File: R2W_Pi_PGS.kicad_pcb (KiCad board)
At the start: 2 copper layers, 33 parts, among them J1 USB_OTG, J2 USB_OTG, U1 PAM2306AYPKE, U2 AP7115-25SEG, U3 DDR2_SODIMM_CM_3_Lite, U4 1040310811

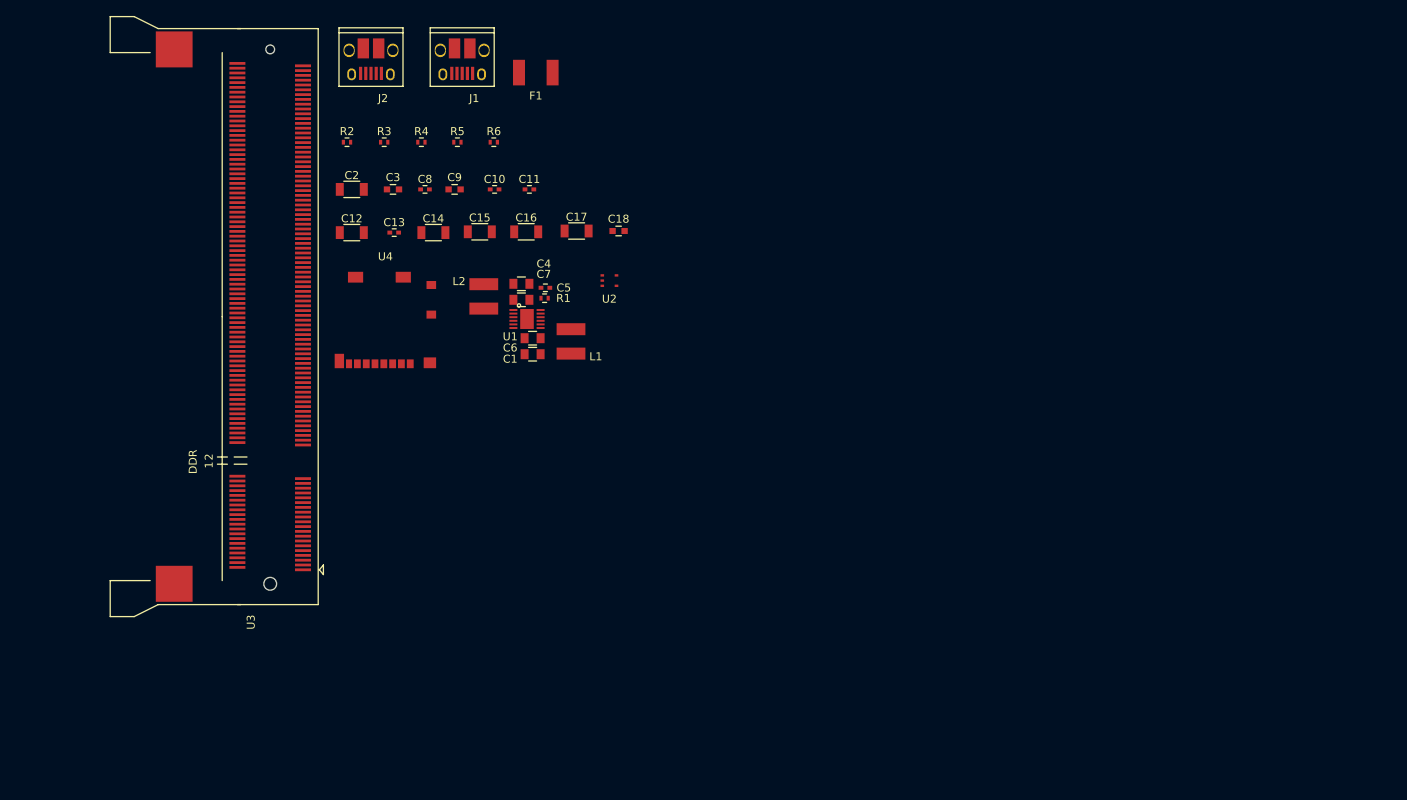
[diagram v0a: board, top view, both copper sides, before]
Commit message: Added screen and buttons
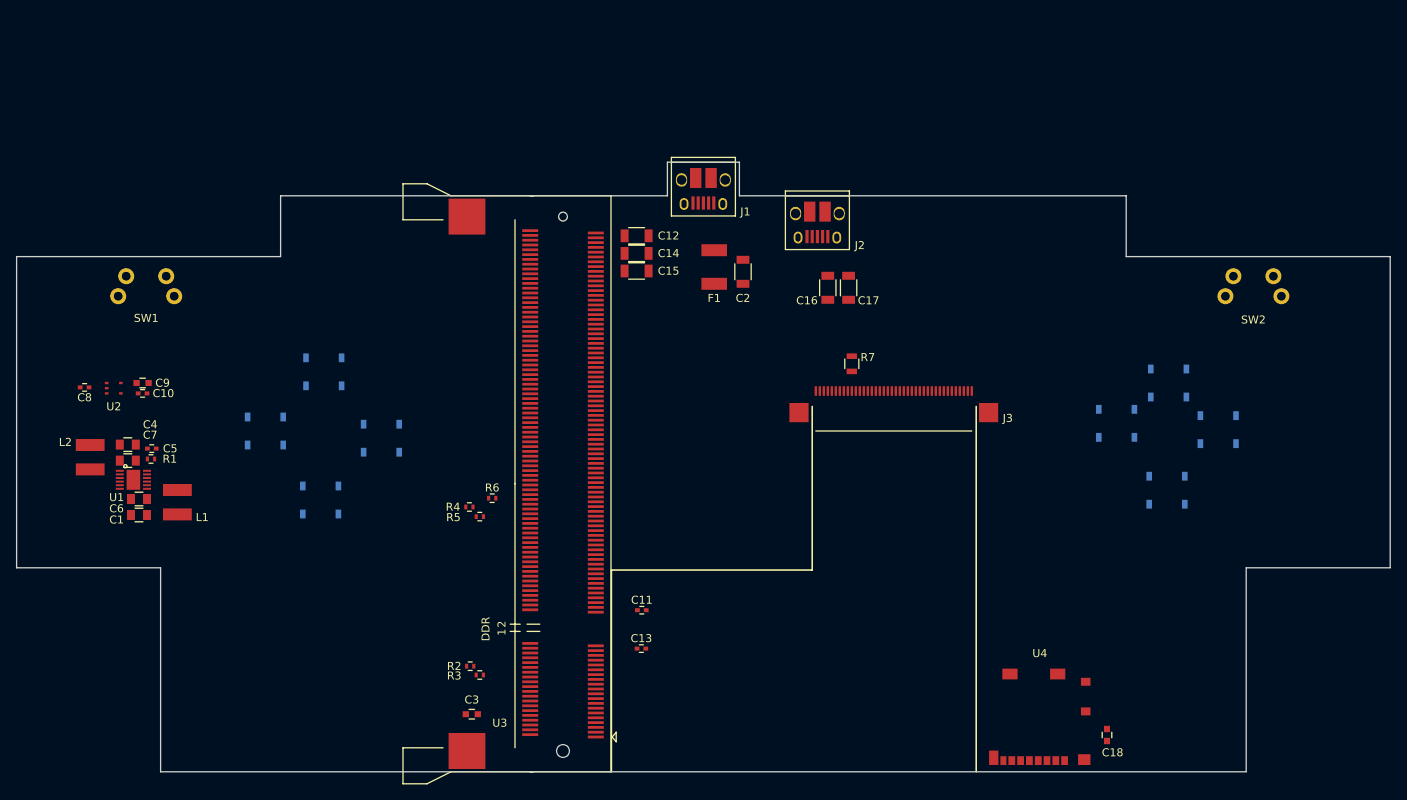
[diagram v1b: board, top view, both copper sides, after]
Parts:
- added J3: 40_Pin_LCD, Pi-Library:LCD_Molex_Connector, F.Cu at (153.9, 97.8)
- added R7: 10k, Resistors_SMD:R_0805, F.Cu at (158.4, 94.4)
- added SW1: R_BUMP, Pi-Library:Tact-switch_right_thru_hole, F.Cu at (70.2, 84.7)
- added SW10: B, Pi-Library:E-SW_SMD, B.Cu at (92.0, 111.4)
- added SW2: L_BUMP, Pi-Library:Tact-switch_right_thru_hole, F.Cu at (208.6, 84.7)
- added SW3: UP, Pi-Library:E-SW_SMD, B.Cu at (198.0, 96.8)
- added SW4: X, Pi-Library:E-SW_SMD, B.Cu at (92.4, 95.4)
- added SW5: LEFT, Pi-Library:E-SW_SMD, B.Cu at (204.2, 102.6)
- added SW6: RIGHT, Pi-Library:E-SW_SMD, B.Cu at (191.5, 101.8)
- added SW7: Y, Pi-Library:E-SW_SMD, B.Cu at (99.6, 103.7)
- added SW8: A, Pi-Library:E-SW_SMD, B.Cu at (85.1, 102.8)
- added SW9: DOWN, Pi-Library:E-SW_SMD, B.Cu at (197.8, 110.2)
- moved U4 95.7 mm to (181.9, 144.0)
- moved C18 87.7 mm to (190.3, 140.8), turned to 270 degrees
- moved R3 67.7 mm to (111.9, 133.3), turned to 180 degrees
- moved R2 67.3 mm to (110.7, 132.2), turned to 180 degrees
- moved C3 66.3 mm to (110.9, 138.2), turned to 180 degrees
- moved U2 63.4 mm to (66.2, 97.5)
- moved C13 60.5 mm to (132.1, 130.0)
- moved J2 59.4 mm to (154.1, 77.0)
- moved C11 54.4 mm to (132.2, 125.2)
- moved L1 53.1 mm to (74.1, 111.7)
- moved L2 53.1 mm to (63.2, 106.1)
- moved U1 53.1 mm to (68.6, 108.9)
- moved C1 53.1 mm to (69.3, 113.3)
- moved C6 53.1 mm to (69.3, 111.3)
- moved R1 53.1 mm to (70.8, 106.3)
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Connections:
- R6 pad 2: GND -> 1V8
- U3 pad 11: Net-(U3-Pad11) -> HSYNC
- U3 pad 15: Net-(U3-Pad15) -> B0
- U3 pad 17: Net-(U3-Pad17) -> B1
- U3 pad 21: Net-(U3-Pad21) -> B2
- U3 pad 23: Net-(U3-Pad23) -> B3
- U3 pad 27: Net-(U3-Pad27) -> B4
- U3 pad 29: Net-(U3-Pad29) -> B5
- U3 pad 3: Net-(U3-Pad3) -> ODCK
- U3 pad 33: Net-(U3-Pad33) -> B6
- U3 pad 35: Net-(U3-Pad35) -> B7
- U3 pad 45: Net-(U3-Pad45) -> G0
- U3 pad 47: Net-(U3-Pad47) -> G1
- U3 pad 5: Net-(U3-Pad5) -> DE
- U3 pad 51: Net-(U3-Pad51) -> G2
- U3 pad 53: Net-(U3-Pad53) -> G3
- U3 pad 57: Net-(U3-Pad57) -> G4
- U3 pad 59: Net-(U3-Pad59) -> G5
- U3 pad 63: Net-(U3-Pad63) -> G6
- U3 pad 65: Net-(U3-Pad65) -> G7
- U3 pad 69: Net-(U3-Pad69) -> R0
- U3 pad 71: Net-(U3-Pad71) -> R1
- U3 pad 75: Net-(U3-Pad75) -> R2
- U3 pad 77: Net-(U3-Pad77) -> R3
- U3 pad 81: Net-(U3-Pad81) -> R4
- U3 pad 83: Net-(U3-Pad83) -> R5
- U3 pad 87: Net-(U3-Pad87) -> R6
- U3 pad 89: Net-(U3-Pad89) -> R7
- U3 pad 9: Net-(U3-Pad9) -> VSYNC
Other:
- board outline added: 171.7 x 76.2 mm
- net class Default: clearance 0.2 -> 0.1524; trace_width 0.25 -> 0.1524; via_dia 0.8 -> 0.6858; via_drill 0.4 -> 0.3302
- rule trace_clearance: 0.2 -> 0.1524
- rule trace_min: 0.2 -> 0.1524
- rule via_min_drill: 0.3 -> 0.254
- rule via_min_size: 0.4 -> 0.508
